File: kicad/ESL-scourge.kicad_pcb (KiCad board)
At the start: 2 copper layers, 80 x 50 mm, 39 parts, among them IC1 MOC3020M, J1 DB9, J2 DB9, P1 CONN_4, P2 CONN_3, P3 CONN_4, Q1 NPN, Q2 NPN, Q3 NPN, U1 TDA2030

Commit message: Bug in pcb fixed
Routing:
- net N-0000022: track 0.00 -> 2.49 mm
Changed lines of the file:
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@@
   (general
     (links 68)
-    (no_connects 1)
-    (area -0.050001 -0.050001 80.050001 50.050001)
+    (no_connects 0)
+    (area -13.832401 -4.2944 93.832401 50.4496)
     (thickness 1.6)
     (drawings 9)
-    (tracks 257)
+    (tracks 259)
     (zones 0)
     (modules 39)
@@
   (segment (start 19.984 19.111) (end 18.8415 19.111) (width 0.3) (layer F.Cu) (net 14))
   (segment (start 18.8415 19.111) (end 17.9525 20) (width 0.3) (layer F.Cu) (net 14))
+  (segment (start 19.984 24.111) (end 19.0635 24.111) (width 0.3) (layer F.Cu) (net 15) (status 400000))
+  (segment (start 19.0635 24.111) (end 17.9525 23) (width 0.3) (layer F.Cu) (net 15) (status 800000))
   (segment (start 51.81 35) (end 51.81 39.81) (width 1) (layer F.Cu) (net 16))
   (segment (start 53.651 41.651) (end 53.651 46) (width 1) (layer F.Cu) (net 16))

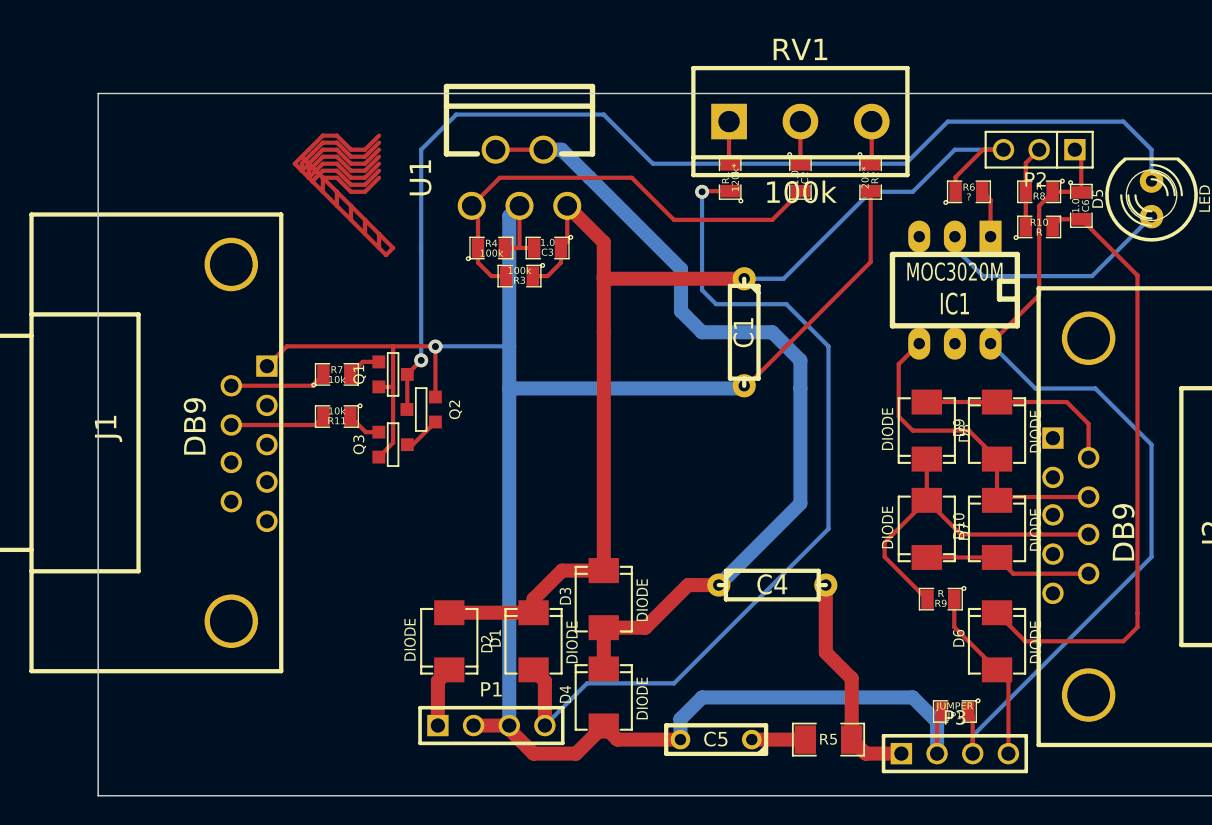
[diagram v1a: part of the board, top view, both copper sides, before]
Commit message: Silks layer corrected
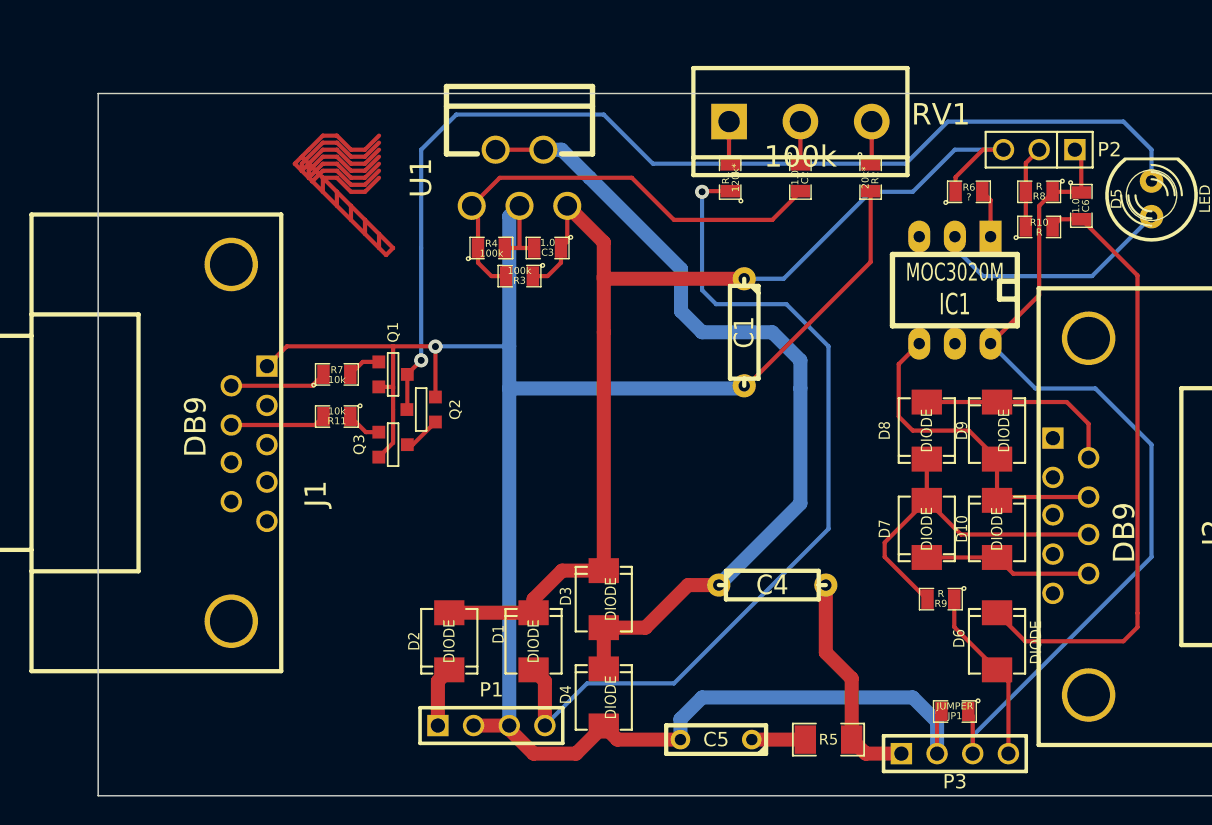
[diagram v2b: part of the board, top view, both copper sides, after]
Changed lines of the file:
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@@
     (links 68)
     (no_connects 0)
-    (area -13.832401 -4.2944 93.832401 50.4496)
+    (area -13.832401 -2.262401 93.832401 50.4496)
     (thickness 1.6)
     (drawings 9)
@@
     (tags "CMS SOT")
     (attr smd)
-    (fp_text reference Q1 (at 0 -2.413 90) (layer F.SilkS)
+    (fp_text reference Q1 (at 3 0 90) (layer F.SilkS)
       (effects (font (size 0.762 0.762) (thickness 0.2032)))
     )
@@
     (descr "Double rangee de contacts 2 x 5 pins")
     (tags CONN)
-    (fp_text reference P3 (at 0 -2.54) (layer F.SilkS)
+    (fp_text reference P3 (at 0 2) (layer F.SilkS)
       (effects (font (size 1.016 1.016) (thickness 0.2032)))
     )
@@
     (descr "Connecteur 3 pins")
     (tags "CONN DEV")
-    (fp_text reference P2 (at 0.254 -2.159 180) (layer F.SilkS)
+    (fp_text reference P2 (at -5 0 180) (layer F.SilkS)
       (effects (font (size 1.016 1.016) (thickness 0.1524)))
     )
@@
     (descr "LED 5mm - Lead pitch 100mil (2,54mm)")
     (tags "LED led 5mm 5MM 100mil 2,54mm")
-    (fp_text reference D5 (at 0 -3.81 90) (layer F.SilkS)
+    (fp_text reference D5 (at 0 -2.5 90) (layer F.SilkS)
       (effects (font (size 0.762 0.762) (thickness 0.0889)))
     )
@@
     (at 59 24 270)
     (attr smd)
-    (fp_text reference D8 (at 0.2 -2.7 270) (layer F.SilkS)
+    (fp_text reference D8 (at 0 3 270) (layer F.SilkS)
       (effects (font (size 0.8 0.7) (thickness 0.15)))
     )
-    (fp_text value DIODE (at -0.088 2.767 270) (layer F.SilkS)
+    (fp_text value DIODE (at 0 0 270) (layer F.SilkS)
       (effects (font (size 0.8 0.7) (thickness 0.15)))
     )
@@
     (at 31 39 90)
     (attr smd)
-    (fp_text reference D1 (at 0.2 -2.7 90) (layer F.SilkS)
+    (fp_text reference D1 (at 0.5 -2.5 90) (layer F.SilkS)
       (effects (font (size 0.8 0.7) (thickness 0.15)))
     )
-    (fp_text value DIODE (at -0.088 2.767 90) (layer F.SilkS)
+    (fp_text value DIODE (at 0 0 90) (layer F.SilkS)
       (effects (font (size 0.8 0.7) (thickness 0.15)))
     )
@@
     (at 25 39 270)
     (attr smd)
-    (fp_text reference D2 (at 0.2 -2.7 270) (layer F.SilkS)
+    (fp_text reference D2 (at 0 2.5 270) (layer F.SilkS)
       (effects (font (size 0.8 0.7) (thickness 0.15)))
     )
-    (fp_text value DIODE (at -0.088 2.767 270) (layer F.SilkS)
+    (fp_text value DIODE (at 0 0 270) (layer F.SilkS)
       (effects (font (size 0.8 0.7) (thickness 0.15)))
     )
@@
       (effects (font (size 0.8 0.7) (thickness 0.15)))
     )
-    (fp_text value DIODE (at -0.088 2.767 90) (layer F.SilkS)
+    (fp_text value DIODE (at 0 0.5 90) (layer F.SilkS)
       (effects (font (size 0.8 0.7) (thickness 0.15)))
     )
@@
       (effects (font (size 0.8 0.7) (thickness 0.15)))
     )
-    (fp_text value DIODE (at -0.088 2.767 90) (layer F.SilkS)
+    (fp_text value DIODE (at 0 0.5 90) (layer F.SilkS)
       (effects (font (size 0.8 0.7) (thickness 0.15)))
     )
@@
     (at 59 31 270)
     (attr smd)
-    (fp_text reference D7 (at 0.2 -2.7 270) (layer F.SilkS)
+    (fp_text reference D7 (at 0 3 270) (layer F.SilkS)
       (effects (font (size 0.8 0.7) (thickness 0.15)))
     )
-    (fp_text value DIODE (at -0.088 2.767 270) (layer F.SilkS)
+    (fp_text value DIODE (at 0 0 270) (layer F.SilkS)
       (effects (font (size 0.8 0.7) (thickness 0.15)))
     )
@@
     (at 64 31 90)
     (attr smd)
-    (fp_text reference D10 (at 0.2 -2.7 90) (layer F.SilkS)
+    (fp_text reference D10 (at 0 -2.5 90) (layer F.SilkS)
       (effects (font (size 0.8 0.7) (thickness 0.15)))
     )
-    (fp_text value DIODE (at -0.088 2.767 90) (layer F.SilkS)
+    (fp_text value DIODE (at 0 0 90) (layer F.SilkS)
       (effects (font (size 0.8 0.7) (thickness 0.15)))
     )
@@
     (at 64 24 90)
     (attr smd)
-    (fp_text reference D9 (at 0.2 -2.7 90) (layer F.SilkS)
+    (fp_text reference D9 (at 0 -2.5 90) (layer F.SilkS)
       (effects (font (size 0.8 0.7) (thickness 0.15)))
     )
-    (fp_text value DIODE (at -0.088 2.767 90) (layer F.SilkS)
+    (fp_text value DIODE (at 0 0.5 90) (layer F.SilkS)
       (effects (font (size 0.8 0.7) (thickness 0.15)))
     )
@@
     (descr "Connecteur DB9 male couche")
     (tags "CONN DB9")
-    (fp_text reference J1 (at 1.27 -10.16 90) (layer F.SilkS)
+    (fp_text reference J1 (at -3.5 4.75 90) (layer F.SilkS)
       (effects (font (size 1.524 1.524) (thickness 0.3048)))
     )
@@
     (descr "Bornier d'alimentation 3 pins")
     (tags DEV)
-    (fp_text reference RV1 (at 0 -5.08) (layer F.SilkS)
+    (fp_text reference RV1 (at 10 -0.5) (layer F.SilkS)
       (effects (font (size 1.524 1.524) (thickness 0.3048)))
     )
-    (fp_text value 100k (at 0 5.08) (layer F.SilkS)
+    (fp_text value 100k (at 0 2.5) (layer F.SilkS)
       (effects (font (size 1.524 1.524) (thickness 0.3048)))
     )
@@
   (segment (start 19.984 19.111) (end 18.8415 19.111) (width 0.3) (layer F.Cu) (net 14))
   (segment (start 18.8415 19.111) (end 17.9525 20) (width 0.3) (layer F.Cu) (net 14))
-  (segment (start 19.984 24.111) (end 19.0635 24.111) (width 0.3) (layer F.Cu) (net 15) (status 400000))
-  (segment (start 19.0635 24.111) (end 17.9525 23) (width 0.3) (layer F.Cu) (net 15) (status 800000))
+  (segment (start 19.984 24.111) (end 19.0635 24.111) (width 0.3) (layer F.Cu) (net 15))
+  (segment (start 19.0635 24.111) (end 17.9525 23) (width 0.3) (layer F.Cu) (net 15))
   (segment (start 51.81 35) (end 51.81 39.81) (width 1) (layer F.Cu) (net 16))
   (segment (start 53.651 41.651) (end 53.651 46) (width 1) (layer F.Cu) (net 16))
@@
   (segment (start 61.0475 5.9525) (end 63 4) (width 0.3) (layer F.Cu) (net 27))
   (segment (start 63 4) (end 64.46 4) (width 0.3) (layer F.Cu) (net 27))
+  (zone (net 0) (net_name "") (layer F.Mask) (hatch edge 0.508)
+    (connect_pads (clearance 0.508))
+    (min_thickness 0.254)
+    (fill (arc_segments 16) (thermal_gap 0.508) (thermal_bridge_width 0.508))
+    (polygon
+      (pts
+        (xy 22 13) (xy 13 13) (xy 13 2) (xy 22 2)
+      )
+    )
+  )
 )

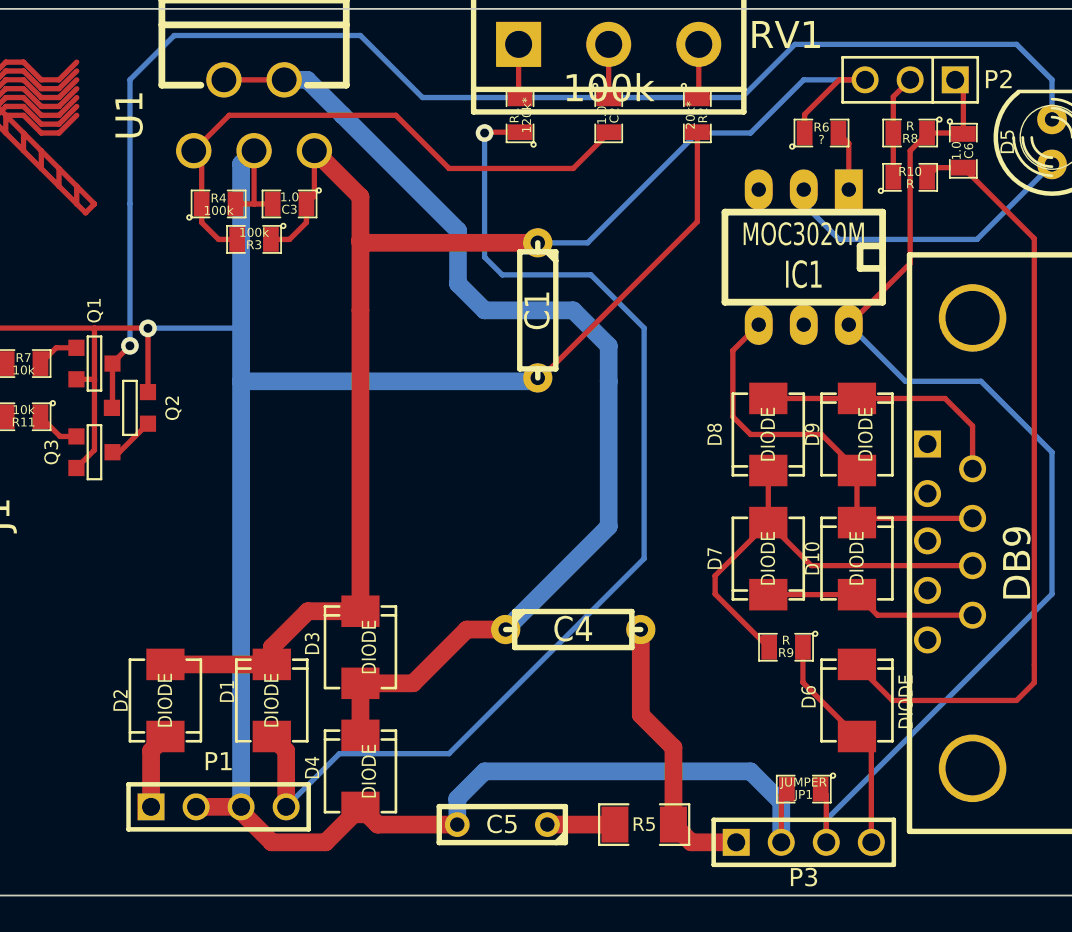
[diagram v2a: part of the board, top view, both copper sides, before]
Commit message: Critical bug fixed in power supply circuit - wrong diode polarity
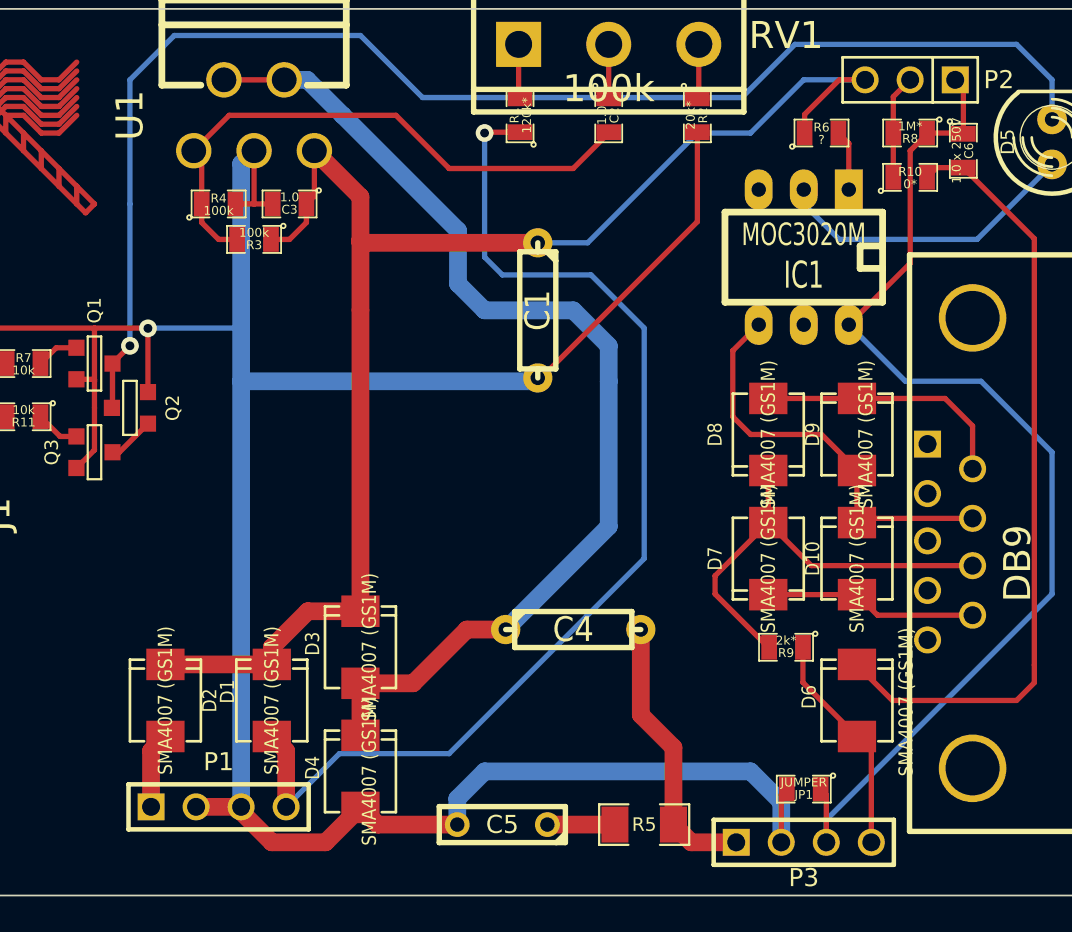
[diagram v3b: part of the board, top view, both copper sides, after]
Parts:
- C6: value 1.0 -> 1.0 x 250V
- D1, D10, D2, D3, D4, D6, D7, D8, D9: value DIODE -> SMA4007 (GS1M)
- Q1, Q2, Q3: value NPN -> BC847
- R10: value R -> 0*
- R8: value R -> 1M*
- R9: value R -> 2k*
- turned D2 to 90 degrees
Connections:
- D2 pad 1: VCC -> N-000004
- D2 pad 2: N-000004 -> VCC

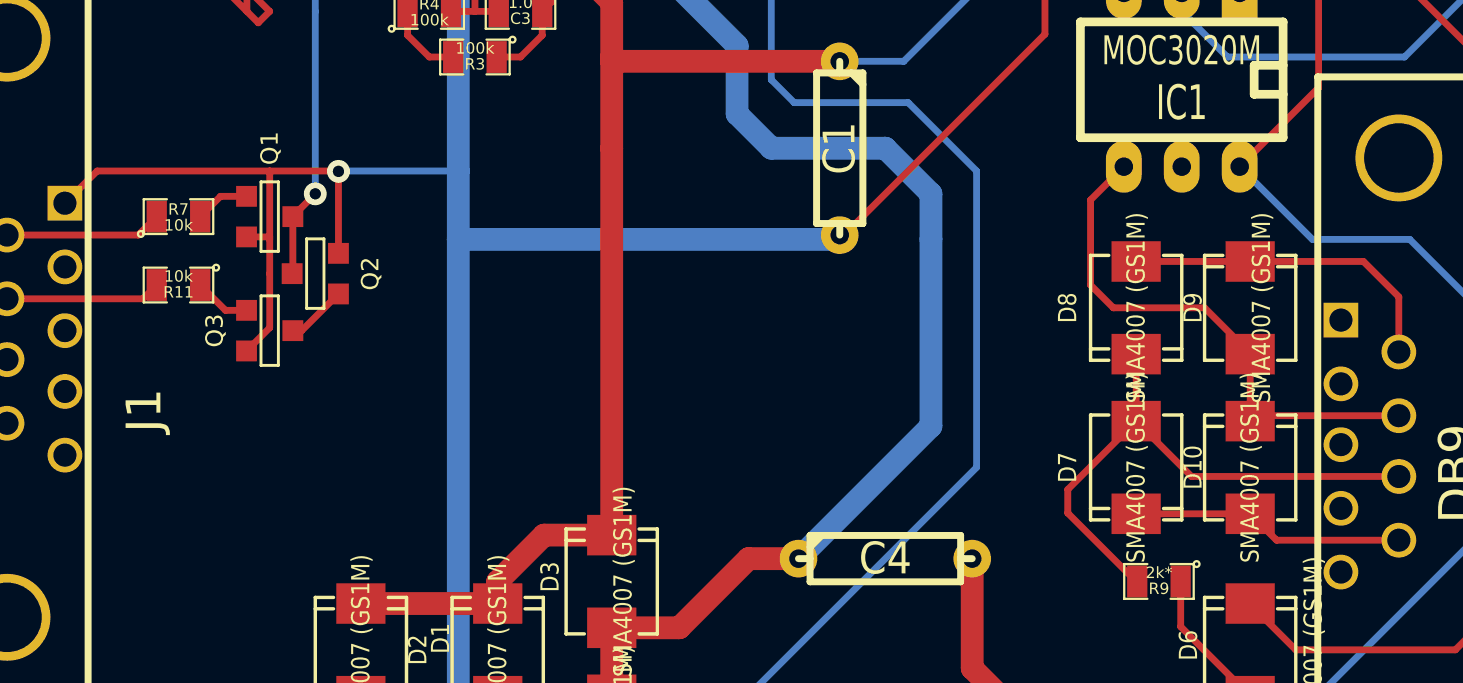
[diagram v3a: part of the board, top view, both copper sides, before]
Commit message: Several critical bugs fixed - wrong diode polarity in output bridge, pullup resistors added in slon-control scheme
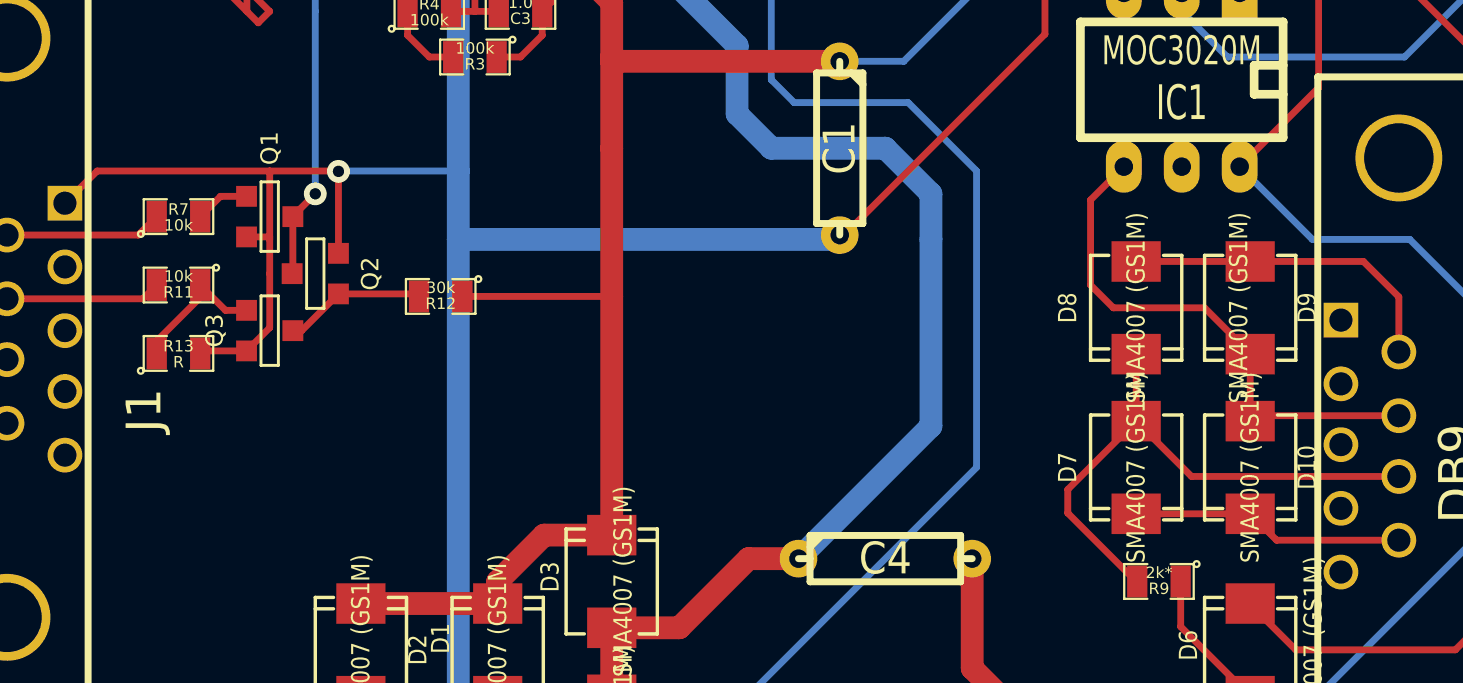
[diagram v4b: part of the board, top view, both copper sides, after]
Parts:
- added R12: 30k, SM0805, F.Cu at (28.5, 23.5)
- added R13: R, SM0805, F.Cu at (17.0, 26.0)
- turned D10 to 270 degrees
- turned D9 to 270 degrees
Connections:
- D10 pad 1: N-0000013 (its old number) -> N-0000032
- D10 pad 2: N-0000033 -> N-000002
- D7 pad 2: N-0000013 (its old number) -> N-000002
- D8 pad 1: N-0000034 -> N-0000031
- D9 pad 1: N-0000033 -> N-0000031
- D9 pad 2: N-0000034 -> N-0000032
- IC1 pad 4: N-0000033 -> N-0000032
- J2 pad 6: N-0000034 -> N-0000031
- J2 pad 7: N-0000033 -> N-0000032
- J2 pad 9: N-0000013 (its old number) -> N-000002
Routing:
- net N-0000033: track 23.6 -> 0.00 mm
- net N-0000032: track 0.00 -> 23.6 mm
- net N-0000034: track 14.6 -> 0.00 mm
- net N-0000031: track 0.00 -> 14.6 mm
- net N-000002: track 0.00 -> 12.0 mm
- net N-0000013 (its old number): track 12.0 -> 0.00 mm
- net VCC: track 84.2 -> 90.8 mm
- net N-0000016: track 2.49 -> 6.28 mm
- net N-0000014: track 2.67 -> 6.24 mm
- net GND: track 151.2 -> 153.3 mm
